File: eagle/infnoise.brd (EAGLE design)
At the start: 31.8 x 12 mm, 25 parts, among them SW1 NS5B1G385DFT2G, SW2 NS5B1G385DFT2G, U1 FT240XQ, X1 USBCON

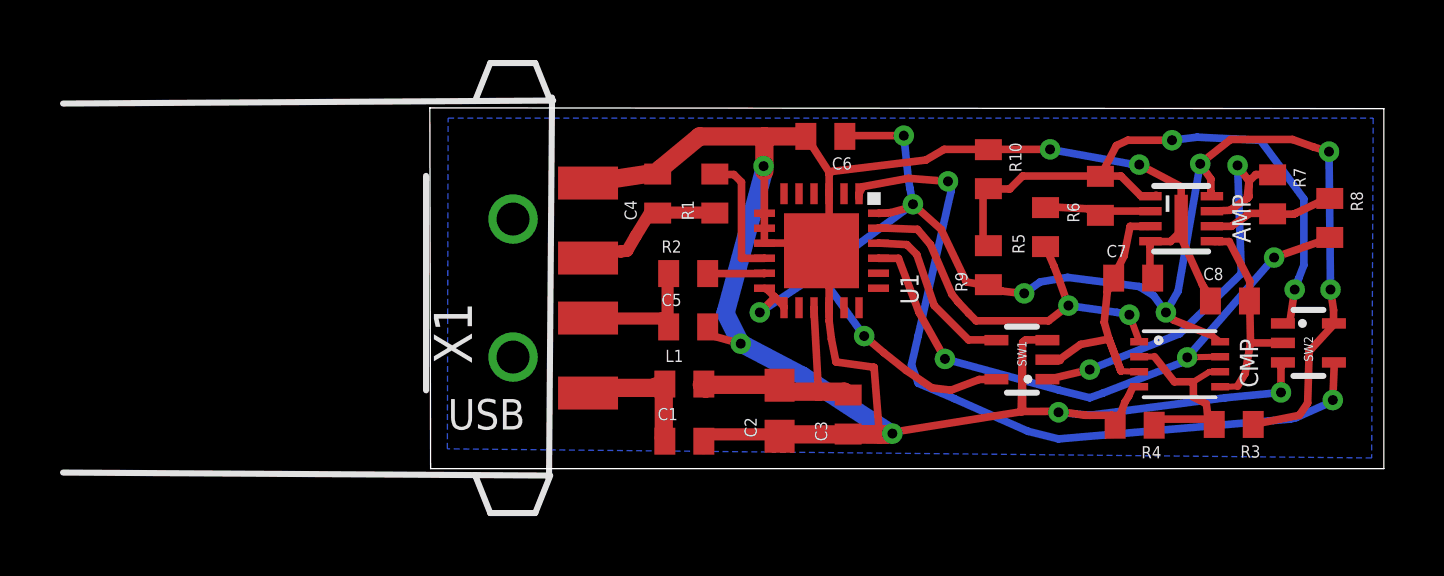
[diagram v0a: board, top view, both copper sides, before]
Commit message: Updated to not extend outside board boundary
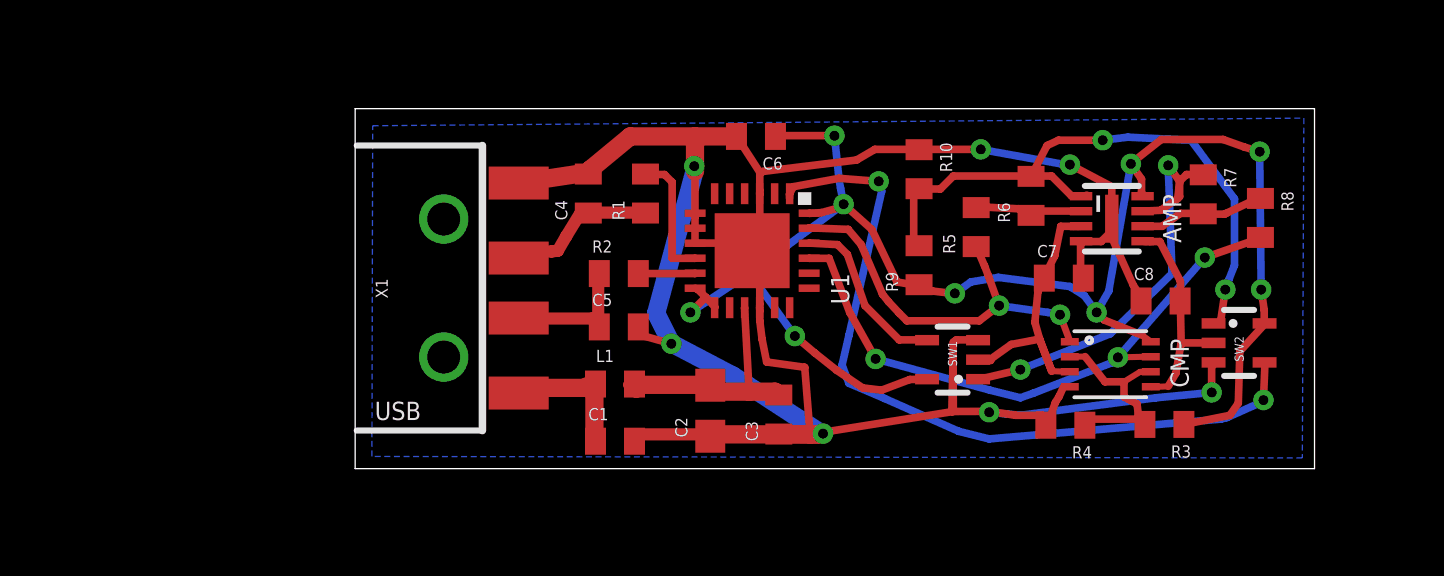
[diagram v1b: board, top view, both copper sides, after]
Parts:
- moved CMP 2.31 mm to (25.2, 3.48)
- moved R3 2.31 mm to (27.0, 1.47)
- moved R4 2.31 mm to (23.7, 1.45)
- moved R7 2.31 mm to (28.3, 9.14)
- moved R8 2.31 mm to (30.2, 8.36)
- moved SW1 2.31 mm to (19.9, 3.63)
- moved SW2 2.31 mm to (29.5, 4.19)
- moved C2 2.31 mm to (11.8, 1.93)
- moved C3 2.31 mm to (14.1, 1.80)
- moved C5 2.31 mm to (8.79, 4.72)
- moved R2 2.31 mm to (8.79, 6.50)
- moved U1 2.31 mm to (13.2, 7.26)
- moved C4 2.31 mm to (7.77, 9.17)
- moved X1 2.31 mm to (6.45, 6.02)
- moved AMP 2.31 mm to (25.2, 8.33)
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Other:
- board size 31.8 x 12 mm -> 32 x 12 mm

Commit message: Modified board to fit USB stick enclosure
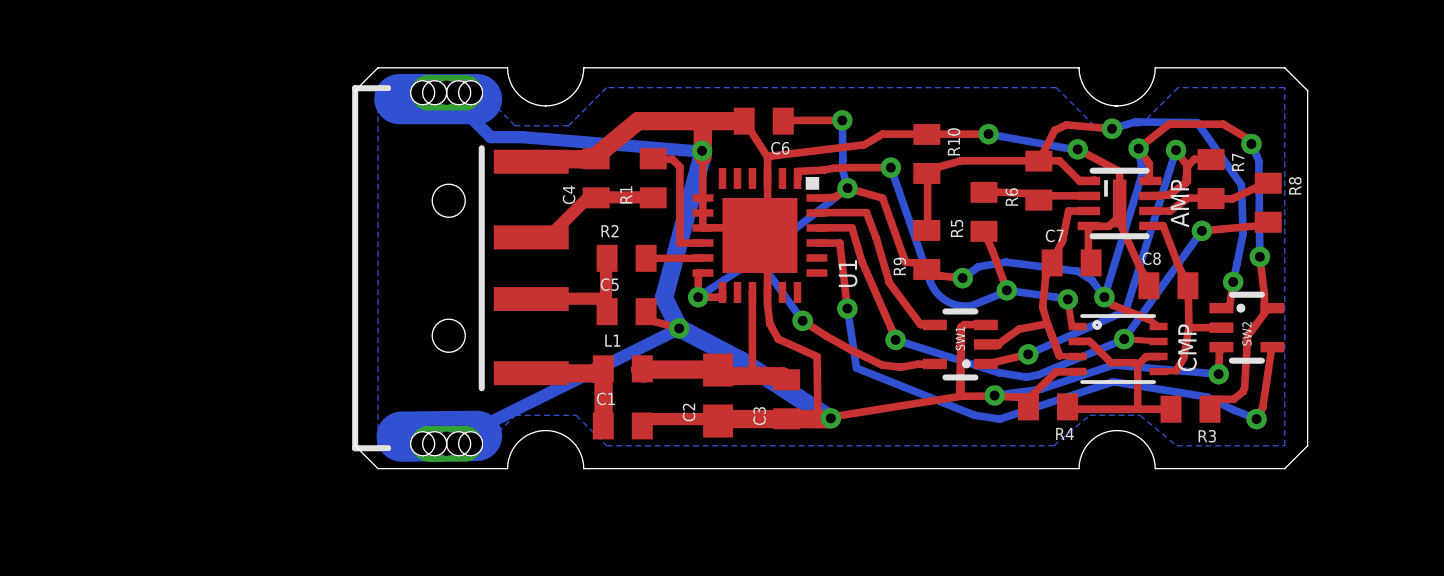
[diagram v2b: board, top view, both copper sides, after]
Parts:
- X1: value USBCON -> USBSMT-MALE; device infnoise:USB-A-CON -> infnoise:USB-A-SMT-MALE
- moved X1 6.49 mm to (0.00, 6.68), turned to 90 degrees
- moved R3 1.01 mm to (27.8, 1.98)
- moved R4 0.84 mm to (23.1, 2.06)
- moved C4 0.57 mm to (8.03, 9.68)
- moved C2 0.57 mm to (12.1, 2.44)
- moved C5 0.57 mm to (9.05, 5.23)
- moved C7 0.57 mm to (23.9, 6.86)
- moved C8 0.57 mm to (27.1, 6.10)
- moved CMP 0.57 mm to (25.4, 3.99)
- moved R1 0.57 mm to (9.94, 9.68)
- moved R2 0.57 mm to (9.05, 7.01)
- moved R9 0.57 mm to (19.1, 7.29)
- moved SW1 0.57 mm to (20.2, 4.14)
- moved SW2 0.57 mm to (29.7, 4.70)
- moved U1 0.57 mm to (13.5, 7.77)
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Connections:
- removed net SW2EN: SW2.4, U1.1
- new net N$1: SW2.4, U1.21
- net COMP1: now also U1.1; no longer U1.23
- net COMP2: now also U1.22; no longer U1.21
- net GND: now also X1.GND1, X1.P$1, X1.P$3; no longer X1.4, X1.H1, X1.H2
- net SW1EN: now also U1.23; no longer U1.22
- net USB_M: now also X1.D+1; no longer X1.3
- net USB_P: now also X1.D-1; no longer X1.2
- net VCC5: now also X1.VBUS1; no longer X1.1
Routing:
- net SW2EN: track 25.8 -> 0.00 mm, vias 2 -> 0
- net GND: track 96.7 -> 118.8 mm
- net N$1: track 0.00 -> 21.6 mm, vias 0 -> 2
- net COMP1: track 13.4 -> 15.5 mm, vias 2 -> 3
- net USB_M: track 6.58 -> 4.63 mm
- net VCC5: track 5.24 -> 4.36 mm
- net VREF: track 7.31 -> 8.12 mm
- net COMP2: track 20.5 -> 21.1 mm
- net SW1EN: track 5.76 -> 6.36 mm
- net USB_P: track 5.18 -> 4.60 mm
- net AMP2OUT: track 15.2 -> 14.6 mm
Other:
- board size 32 x 12 mm -> 31.8 x 13.4 mm

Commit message: Converted to 0603 parts to be compatible with Small Batch Assembly
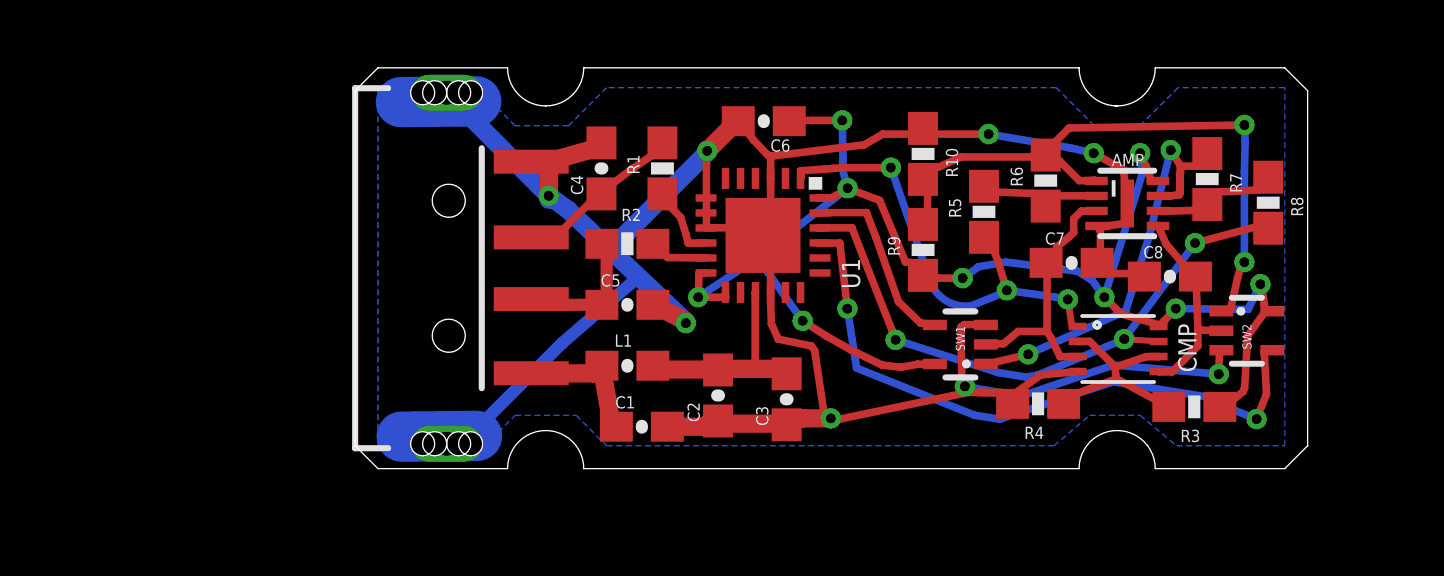
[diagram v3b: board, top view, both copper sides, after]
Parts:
- C1, C3, C4, C5, C6, C7, C8: device infnoise:0402-CAP -> infnoise:0603-CAP
- L1: value CIM05U601NC -> FERRITE-BEAD0603-IND; device infnoise:0402 -> infnoise:0603-IND
- R1, R10, R2, R3, R4, R5, R6, R7, R8, R9: device infnoise:0402-RES -> infnoise:0603-RES
- moved C1 0.64 mm to (9.56, 1.40)
- moved R2 0.48 mm to (9.07, 7.49)
- moved R1 0.45 mm to (10.2, 10.0)
- moved C4 0.38 mm to (8.21, 10.0)
- moved R4 0.35 mm to (22.8, 2.16)
- moved C8 0.31 mm to (27.2, 6.40)
- moved AMP 0.25 mm to (25.7, 8.84)
- moved C5 0.23 mm to (9.07, 5.46)
- moved R6 0.23 mm to (23.0, 9.60)
- moved L1 0.18 mm to (9.07, 3.43)
- moved R3 0.15 mm to (28.0, 2.06)
- moved R10 0.13 mm to (18.9, 10.5)
- moved R7 0.13 mm to (28.4, 9.65)
- moved R9 0.13 mm to (18.9, 7.29)
- moved SW2 0.10 mm to (29.7, 4.60)
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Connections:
- removed net USBDP: R1.2, U1.10
- new net N$2: R1.1, U1.10
- net USB_M: now also R1.2; no longer R1.1
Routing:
- net GND: track 118.8 -> 100.4 mm, vias 7 -> 8
- net USBDP: track 4.30 -> 0.00 mm
- net VCC33: track 55.4 -> 51.7 mm
- net N$2: track 0.00 -> 2.51 mm
- net AMP1OUT: track 21.5 -> 23.5 mm
- net A: track 10.6 -> 8.85 mm
- net USB_M: track 4.63 -> 5.77 mm
- net AMP2OUT: track 14.6 -> 15.6 mm
- net VCC: track 8.23 -> 9.19 mm
- net FB2: track 4.19 -> 4.91 mm
- net FB1: track 3.68 -> 4.35 mm

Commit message: move a wire
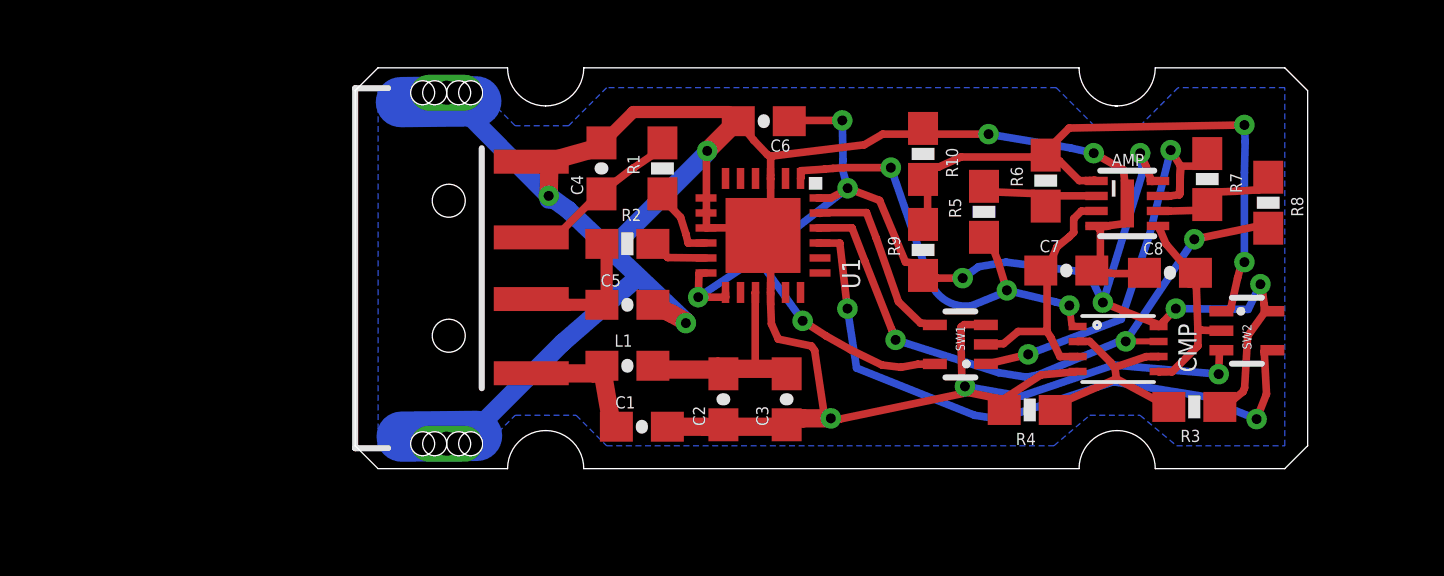
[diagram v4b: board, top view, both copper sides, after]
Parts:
- moved R4 0.35 mm to (22.5, 1.96)
- moved C7 0.31 mm to (23.7, 6.60)
- moved C2 0.22 mm to (12.3, 2.31)
- moved C8 0.13 mm to (27.2, 6.53)
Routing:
- net GND: track 100.4 -> 105.0 mm
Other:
- board text added: "Infinite Noise"

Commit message: Updated driver to use correct pins
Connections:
- net N$1 renamed SW2EN
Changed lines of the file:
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@@
 <grid distance="0.001" unitdist="inch" unit="inch" style="lines" multiple="1" display="no" altdistance="0.025" altunitdist="inch" altunit="inch"/>
 <layers>
-<layer number="1" name="Top" color="4" fill="1" visible="no" active="yes"/>
+<layer number="1" name="Top" color="4" fill="1" visible="yes" active="yes"/>
 <layer number="16" name="Bottom" color="1" fill="1" visible="no" active="yes"/>
-<layer number="17" name="Pads" color="2" fill="1" visible="no" active="yes"/>
-<layer number="18" name="Vias" color="2" fill="1" visible="no" active="yes"/>
-<layer number="19" name="Unrouted" color="6" fill="1" visible="no" active="yes"/>
+<layer number="17" name="Pads" color="2" fill="1" visible="yes" active="yes"/>
+<layer number="18" name="Vias" color="2" fill="1" visible="yes" active="yes"/>
+<layer number="19" name="Unrouted" color="6" fill="1" visible="yes" active="yes"/>
 <layer number="20" name="Dimension" color="15" fill="1" visible="yes" active="yes"/>
-<layer number="21" name="tPlace" color="7" fill="1" visible="no" active="yes"/>
-<layer number="22" name="bPlace" color="7" fill="1" visible="no" active="yes"/>
-<layer number="23" name="tOrigins" color="15" fill="1" visible="no" active="yes"/>
-<layer number="24" name="bOrigins" color="15" fill="1" visible="no" active="yes"/>
-<layer number="25" name="tNames" color="7" fill="1" visible="no" active="yes"/>
+<layer number="21" name="tPlace" color="7" fill="1" visible="yes" active="yes"/>
+<layer number="22" name="bPlace" color="7" fill="1" visible="yes" active="yes"/>
+<layer number="23" name="tOrigins" color="15" fill="1" visible="yes" active="yes"/>
+<layer number="24" name="bOrigins" color="15" fill="1" visible="yes" active="yes"/>
+<layer number="25" name="tNames" color="7" fill="1" visible="yes" active="yes"/>
 <layer number="26" name="bNames" color="7" fill="1" visible="yes" active="yes"/>
-<layer number="27" name="tValues" color="7" fill="1" visible="no" active="yes"/>
-<layer number="28" name="bValues" color="7" fill="1" visible="no" active="yes"/>
-<layer number="29" name="tStop" color="7" fill="3" visible="no" active="yes"/>
-<layer number="30" name="bStop" color="7" fill="6" visible="no" active="yes"/>
-<layer number="31" name="tCream" color="7" fill="4" visible="no" active="yes"/>
-<layer number="32" name="bCream" color="7" fill="5" visible="no" active="yes"/>
-<layer number="33" name="tFinish" color="6" fill="3" visible="no" active="yes"/>
-<layer number="34" name="bFinish" color="6" fill="6" visible="no" active="yes"/>
-<layer number="35" name="tGlue" color="7" fill="4" visible="no" active="yes"/>
-<layer number="36" name="bGlue" color="7" fill="5" visible="no" active="yes"/>
-<layer number="37" name="tTest" color="7" fill="1" visible="no" active="yes"/>
-<layer number="38" name="bTest" color="7" fill="1" visible="no" active="yes"/>
-<layer number="39" name="tKeepout" color="4" fill="11" visible="no" active="yes"/>
-<layer number="40" name="bKeepout" color="1" fill="11" visible="no" active="yes"/>
-<layer number="41" name="tRestrict" color="4" fill="10" visible="no" active="yes"/>
-<layer number="42" name="bRestrict" color="1" fill="10" visible="no" active="yes"/>
-<layer number="43" name="vRestrict" color="2" fill="10" visible="no" active="yes"/>
-<layer number="44" name="Drills" color="7" fill="1" visible="no" active="yes"/>
-<layer number="45" name="Holes" color="7" fill="1" visible="no" active="yes"/>
-<layer number="46" name="Milling" color="3" fill="1" visible="no" active="yes"/>
-<layer number="47" name="Measures" color="7" fill="1" visible="no" active="yes"/>
-<layer number="48" name="Document" color="7" fill="1" visible="no" active="yes"/>
-<layer number="49" name="Reference" color="7" fill="1" visible="no" active="yes"/>
-<layer number="51" name="tDocu" color="7" fill="1" visible="no" active="yes"/>
-<layer number="52" name="bDocu" color="7" fill="1" visible="no" active="yes"/>
+<layer number="27" name="tValues" color="7" fill="1" visible="yes" active="yes"/>
+<layer number="28" name="bValues" color="7" fill="1" visible="yes" active="yes"/>
+<layer number="29" name="tStop" color="7" fill="3" visible="yes" active="yes"/>
+<layer number="30" name="bStop" color="7" fill="6" visible="yes" active="yes"/>
+<layer number="31" name="tCream" color="7" fill="4" visible="yes" active="yes"/>
+<layer number="32" name="bCream" color="7" fill="5" visible="yes" active="yes"/>
+<layer number="33" name="tFinish" color="6" fill="3" visible="yes" active="yes"/>
+<layer number="34" name="bFinish" color="6" fill="6" visible="yes" active="yes"/>
+<layer number="35" name="tGlue" color="7" fill="4" visible="yes" active="yes"/>
+<layer number="36" name="bGlue" color="7" fill="5" visible="yes" active="yes"/>
+<layer number="37" name="tTest" color="7" fill="1" visible="yes" active="yes"/>
+<layer number="38" name="bTest" color="7" fill="1" visible="yes" active="yes"/>
+<layer number="39" name="tKeepout" color="4" fill="11" visible="yes" active="yes"/>
+<layer number="40" name="bKeepout" color="1" fill="11" visible="yes" active="yes"/>
+<layer number="41" name="tRestrict" color="4" fill="10" visible="yes" active="yes"/>
+<layer number="42" name="bRestrict" color="1" fill="10" visible="yes" active="yes"/>
+<layer number="43" name="vRestrict" color="2" fill="10" visible="yes" active="yes"/>
+<layer number="44" name="Drills" color="7" fill="1" visible="yes" active="yes"/>
+<layer number="45" name="Holes" color="7" fill="1" visible="yes" active="yes"/>
+<layer number="46" name="Milling" color="3" fill="1" visible="yes" active="yes"/>
+<layer number="47" name="Measures" color="7" fill="1" visible="yes" active="yes"/>
+<layer number="48" name="Document" color="7" fill="1" visible="yes" active="yes"/>
+<layer number="49" name="Reference" color="7" fill="1" visible="yes" active="yes"/>
+<layer number="51" name="tDocu" color="7" fill="1" visible="yes" active="yes"/>
+<layer number="52" name="bDocu" color="7" fill="1" visible="yes" active="yes"/>
 <layer number="90" name="Modules" color="5" fill="1" visible="no" active="no"/>
 <layer number="91" name="Nets" color="2" fill="1" visible="no" active="no"/>
@@
 <wire x1="10.4204" y1="7.0358" x2="11.6954" y2="7.0224" width="0.254" layer="1"/>
 </signal>
-<signal name="N$1">
+<signal name="SW2EN">
 <contactref element="SW2" pad="4"/>
 <contactref element="U1" pad="21"/>

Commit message: tweaks
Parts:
- R6, R7: value 8.2K -> 9.76K
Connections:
- removed net VCC5: C1.1, L1.1, X1.VBUS1
- new net VCCIN: C1.1, L1.1, X1.1
- net GND: now also X1.4; no longer X1.GND1
- net USB_M: now also C5.1, R2.1, X1.2; no longer C4.1, R1.2, X1.D+1
- net USB_P: now also C4.1, R1.2, X1.3; no longer C5.1, R2.1, X1.D-1
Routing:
- net GND: track 105.0 -> 110.7 mm
- net VCC5: track 4.61 -> 0.00 mm
- net VCCIN: track 0.00 -> 4.58 mm
- net USB_M: track 5.77 -> 4.67 mm
- net USB_P: track 4.72 -> 5.74 mm
- net VCC33: track 51.9 -> 51.3 mm
